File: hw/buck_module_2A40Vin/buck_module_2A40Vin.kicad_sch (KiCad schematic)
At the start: 22 parts, among them IC1 LV14240DDAR, J1 Conn_01x06, J2 Conn_01x06

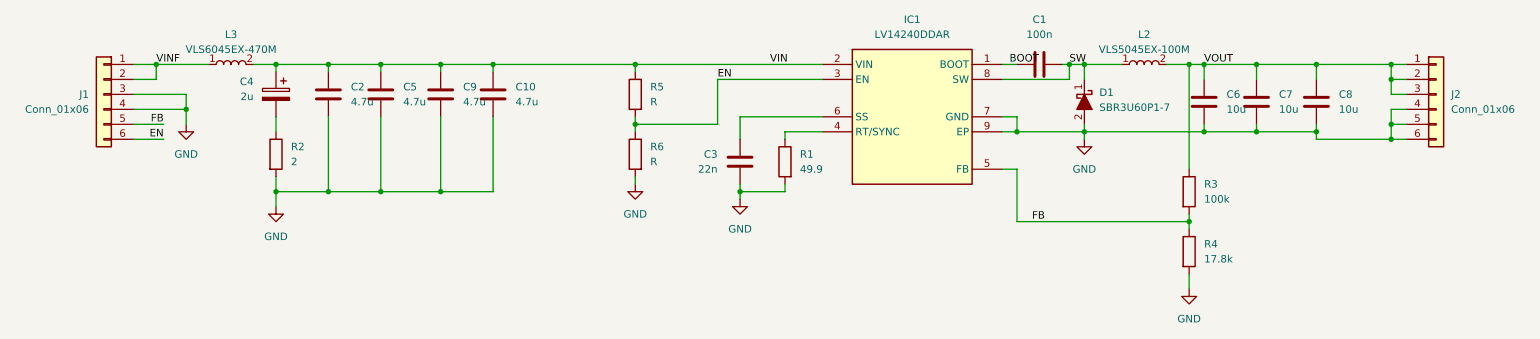
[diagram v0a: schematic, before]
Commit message: Added Simplis simulation for input filter design
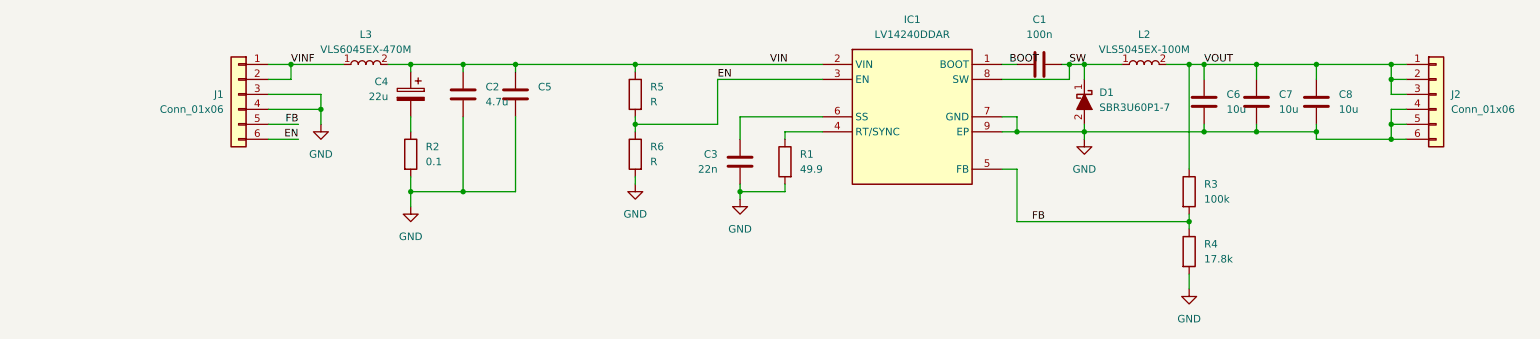
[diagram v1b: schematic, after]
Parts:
- removed C10, C9: 4.7u, Capacitor_SMD:C_0805_2012Metric, symbol 03_GenericPassives:Cap_0805
- C4: value 2u -> 22u
- R2: value 2 -> 0.1
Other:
- moved on the sheet: C2, C4, C5, J1, L3, R2
